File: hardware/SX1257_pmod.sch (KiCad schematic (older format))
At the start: 43 parts, among them J1 Conn_02x06_Odd_Even, J2 SMA_F_RX, J3 SMA_F_TX, U1 SX1257, Y1 32/36MHz ?ppm

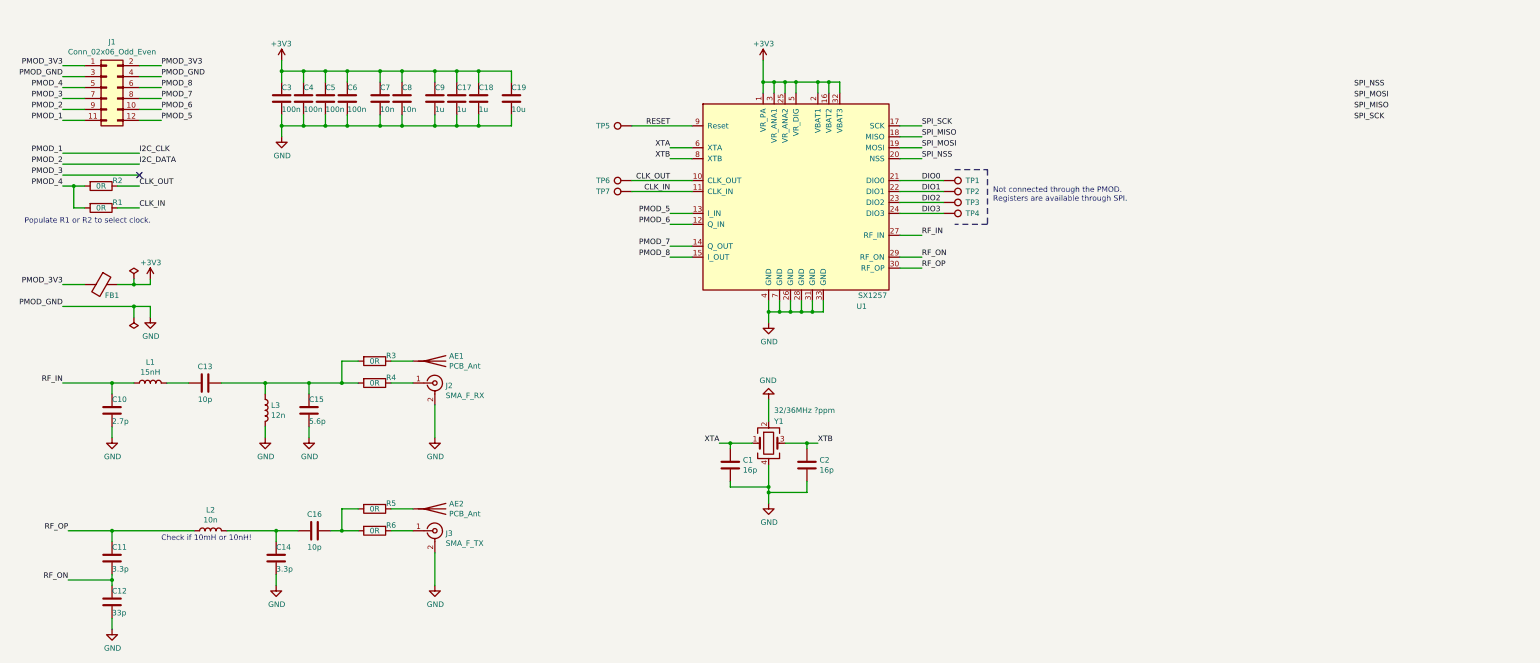
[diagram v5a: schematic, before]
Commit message: Initial PCB routing
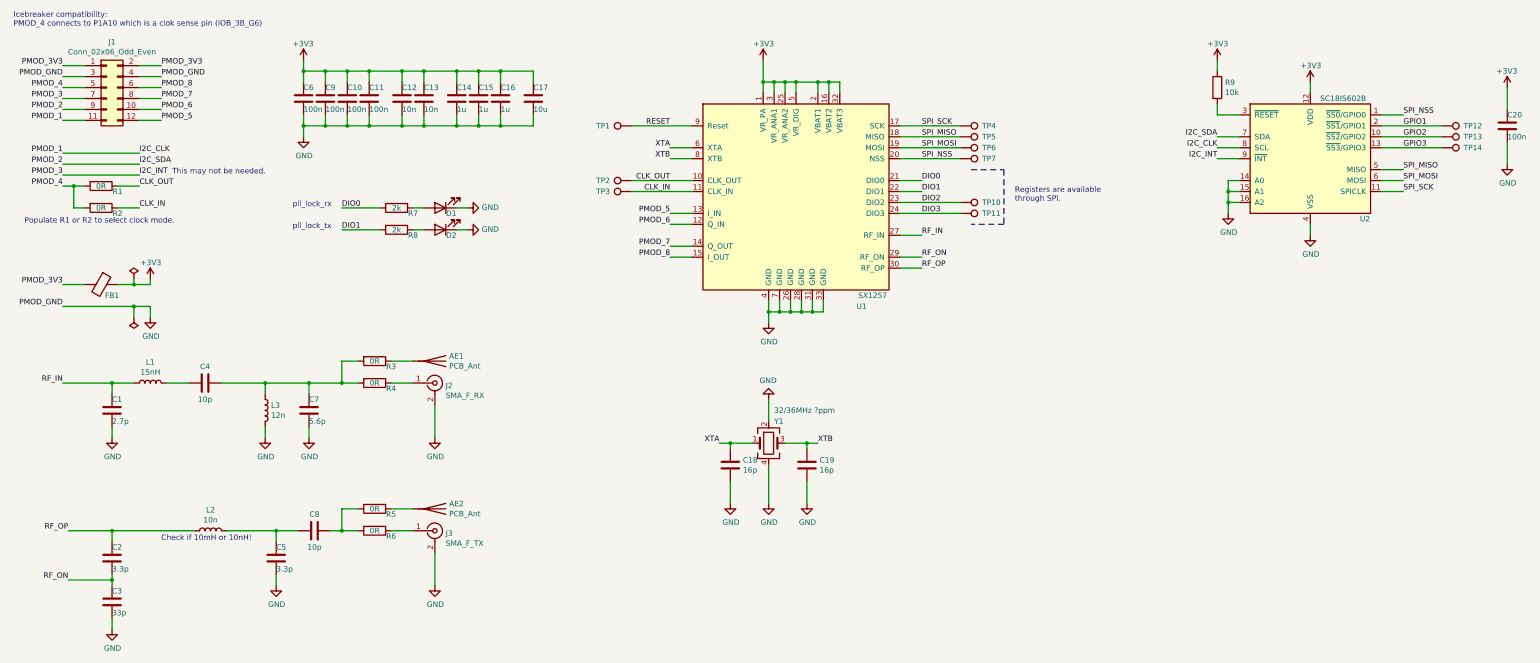
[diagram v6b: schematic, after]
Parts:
- removed TP1, TP2: TestPoint, symbol Connector:TestPoint
- added C20: 100n, Capacitor_SMD:C_0603_1608Metric, symbol Device:C
- added D1, D2: LED, LED_SMD:LED_0603_1608Metric, symbol Device:LED
- added R7, R8: 2k, Resistor_SMD:R_0603_1608Metric, symbol Device:R
- added R9: 10k, Resistor_SMD:R_0603_1608Metric, symbol Device:R
- added TP12, TP13, TP14, TP4, TP5, TP6, TP7: TestPoint, TestPoint:TestPoint_Pad_D1.0mm, symbol Connector:TestPoint
- added U2: SC18IS602B, Package_SO:TSSOP-16_4.4x5mm_P0.65mm, symbol SC18IS602B:SC18IS602B
- C1: renamed from C10; footprint (none) -> Capacitor_SMD:C_0603_1608Metric
- C10: renamed from C5; footprint (none) -> Capacitor_SMD:C_0603_1608Metric
- C11: renamed from C6; footprint (none) -> Capacitor_SMD:C_0603_1608Metric
- C12: renamed from C7; footprint (none) -> Capacitor_SMD:C_0603_1608Metric
- C13: renamed from C8; footprint (none) -> Capacitor_SMD:C_0603_1608Metric
- C14: renamed from C9; footprint (none) -> Capacitor_SMD:C_0603_1608Metric
- C15: renamed from C17; footprint (none) -> Capacitor_SMD:C_0603_1608Metric
- C16: renamed from C18; footprint (none) -> Capacitor_SMD:C_0603_1608Metric
- C17: renamed from C19; footprint (none) -> Capacitor_SMD:C_0603_1608Metric
- C18: renamed from C1; footprint (none) -> Capacitor_SMD:C_0603_1608Metric
- C19: renamed from C2; footprint (none) -> Capacitor_SMD:C_0603_1608Metric
- C2: renamed from C11; footprint (none) -> Capacitor_SMD:C_0603_1608Metric
- C3: renamed from C12; footprint (none) -> Capacitor_SMD:C_0603_1608Metric
- C4: renamed from C13; footprint (none) -> Capacitor_SMD:C_0603_1608Metric
- C5: renamed from C14; footprint (none) -> Capacitor_SMD:C_0603_1608Metric
- C6: renamed from C3; footprint (none) -> Capacitor_SMD:C_0603_1608Metric
- C7: renamed from C15; footprint (none) -> Capacitor_SMD:C_0603_1608Metric
- C8: renamed from C16; footprint (none) -> Capacitor_SMD:C_0603_1608Metric
- C9: renamed from C4; footprint (none) -> Capacitor_SMD:C_0603_1608Metric
- FB1, L1, L2, L3: footprint (none) -> Inductor_SMD:L_0603_1608Metric
- J2, J3: footprint (none) -> Connector_Coaxial:SMA_Amphenol_132134-10_Vertical
- R1: renamed from R2; footprint (none) -> Resistor_SMD:R_0603_1608Metric
- R2: renamed from R1; footprint (none) -> Resistor_SMD:R_0603_1608Metric
- R3, R4, R5, R6: footprint (none) -> Resistor_SMD:R_0603_1608Metric
- TP1: renamed from TP5; footprint (none) -> TestPoint:TestPoint_Pad_D1.0mm
- TP10: renamed from TP3; footprint (none) -> TestPoint:TestPoint_Pad_D1.0mm
- TP11: renamed from TP4; footprint (none) -> TestPoint:TestPoint_Pad_D1.0mm
- TP2: renamed from TP6; footprint (none) -> TestPoint:TestPoint_Pad_D1.0mm
- TP3: renamed from TP7; footprint (none) -> TestPoint:TestPoint_Pad_D1.0mm
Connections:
- net +3V3: now also C20.1, R9.1, U2.12 (VDD)
- net DIO0: now also R7.2
- net DIO1: now also R8.2
- net GND: now also C20.2, D1.1 (K), D2.1 (K), U2.14 (A0), U2.15 (A1), U2.16 (A2), U2.4 (VSS)
- net I2C_CLK: now also U2.8 (SCL)
- net SPI_MISO: now also TP5.1, U2.5 (MISO)
- net SPI_MOSI: now also TP6.1, U2.6 (MOSI)
- net SPI_NSS: now also TP7.1, U2.1 (~SS0~/GPIO0)
- net SPI_SCK: now also TP4.1, U2.11 (SPICLK)
- net I2C_DATA renamed I2C_SDA
- net I2C_SDA: now also U2.7 (SDA)
- net PMOD_3 renamed I2C_INT
- net I2C_INT: now also U2.9 (~INT~)
- new net: R9.2, U2.3 (~RESET~)
- new net: D1.2 (A), R7.1
- new net: D2.2 (A), R8.1
- new net GPIO1: TP12.1, U2.2 (~SS1~/GPIO1)
- new net GPIO2: TP13.1, U2.10 (~SS2~/GPIO2)
- new net GPIO3: TP14.1, U2.13 (~SS3~/GPIO3)
- no-connect marks 1 -> 0
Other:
- note added: "Icebreaker compatibility:\nPMOD_4 connects to P1A10 which is a clok sense pin (IOB_3B_G6)"
- note added: "Populate R1 or R2 to select clock mode."
- note added: "Registers are available\nthrough SPI."
- note added: "This may not be needed."
- note added: "pll_lock_rx"
- note added: "pll_lock_tx"
- note removed: "Not connected through the PMOD.\nRegisters are available through SPI."
- note removed: "Populate R1 or R2 to select clock."
- moved on the sheet: C10, C11, C12, C13, C14, C15, C16, C17, C6, C9, TP10, TP11

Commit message: Fix typo
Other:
- note added: "Icebreaker compatibility:\nPMOD_4 connects to P1A10 which is a global/clock input pin (IOB_3B_G6)"
- note removed: "Icebreaker compatibility:\nPMOD_4 connects to P1A10 which is a clok sense pin (IOB_3B_G6)"
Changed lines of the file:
@@
 This may not be needed.
 Text Notes 550  700  0    50   ~ 0
-Icebreaker compatibility:\nPMOD_4 connects to P1A10 which is a clok sense pin (IOB_3B_G6)
+Icebreaker compatibility:\nPMOD_4 connects to P1A10 which is a global/clock input pin (IOB_3B_G6)
 Text Label 3550 2350 0    50   ~ 0
 DIO0
